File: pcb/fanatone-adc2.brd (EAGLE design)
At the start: 49 x 32 mm, 71 parts, among them IC1 OPA2134U, IC2 DIT4192-H, IC3 PCM4201-TSSOP-16, IC4 OPA2134U, Q1 SST5484, U1 OPA1612AID, U2 TPS62240DRVTG4

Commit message: Dickson charge pump layout, PCB wip, tidy up
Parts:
- removed C31: 0.1uF, SparkFun-Capacitors:0402-CAP
- added C33: 1uF, SparkFun-Passives:0805
- added D17: PMEG4005EJ, SparkFun-DiscreteSemi:SOD523
- added R10: 24k9, SparkFun-Passives:0603-RES
- added R9: 1M, SparkFun-Passives:0603-RES
- C22: value 1uF -> 1uF 16V
- C23: value 4.7uF 63V -> 4.7uF 16V
- D10, D11, D12, D13, D14, D15, D4, D5, D6, D7, D8, D9: device SparkFun-DiscreteSemi:SOD-323 -> SparkFun-DiscreteSemi:SOD523
- L1: value 4.7uH -> 1uH
- moved C32 134.6 mm to (74.7, 19.3), turned to 90 degrees
- moved C30 130.8 mm to (74.7, 22.9), turned to 270 degrees
- moved C25 124.1 mm to (85.1, 16.0), turned to 90 degrees
- moved U$5 123.7 mm to (71.9, 21.1), turned to 180 degrees
- moved C26 120.0 mm to (82.5, 16.0), turned to 90 degrees
- moved C29 119.5 mm to (74.9, 16.0), turned to 90 degrees
- moved D10 118.1 mm to (88.4, 14.2)
- moved C24 116.6 mm to (87.6, 16.0), turned to 90 degrees
- moved D12 116.4 mm to (83.3, 14.2)
- moved C27 116.0 mm to (80.0, 16.0), turned to 90 degrees
- moved C21 115.1 mm to (89.7, 10.9), turned to 270 degrees
- moved D14 115.1 mm to (78.2, 14.2)
- moved D9 112.9 mm to (88.4, 12.7), turned to 180 degrees
- moved C28 112.1 mm to (77.5, 16.0), turned to 90 degrees
- moved D11 112.0 mm to (85.9, 14.2)
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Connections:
- removed net N$35: C30.1, U$5.1
- new net N$32: C29.1, D15.C, D17.A
- net GND: now also C32.2, C33.2, R10.1
- net N$34: now also R10.2, R9.1, U$5.2; no longer U$5.8
- net N$38: now also D16.C
- net N$49: now also C33.1, D17.C, U$5.8; no longer C29.1, D15.C
- net VCAPSULE-RAW: now also C30.1, R9.2, U$5.1
- net VDPP: now also D16.A
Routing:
- net GND: track 57.0 -> 74.4 mm
- net N$34: track 0.00 -> 4.73 mm
- net N$38: track 0.00 -> 4.46 mm
- net N$48: track 0.00 -> 2.51 mm
- net N$46: track 0.00 -> 2.51 mm
- net N$41: track 0.00 -> 2.51 mm
- net N$47: track 0.00 -> 2.51 mm
- net N$43: track 0.00 -> 2.51 mm
- net N$32: track 0.00 -> 2.51 mm
- net N$29: track 0.00 -> 2.46 mm
- net N$36: track 0.00 -> 2.46 mm
- net N$33: track 0.00 -> 2.46 mm
- net N$27: track 0.00 -> 2.46 mm
- net N$13: track 0.00 -> 2.46 mm
- net VCAPSULE-RAW: track 8.09 -> 10.5 mm
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
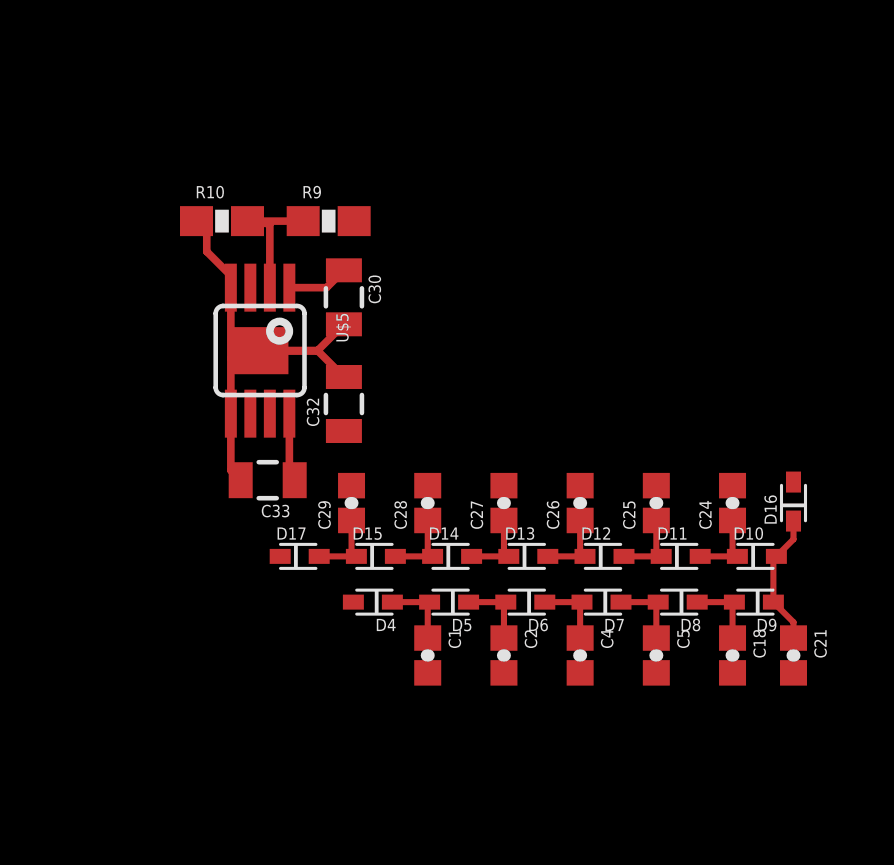
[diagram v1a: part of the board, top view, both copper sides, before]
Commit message: add concept for a MEMS Microphone array + step file sync + animation
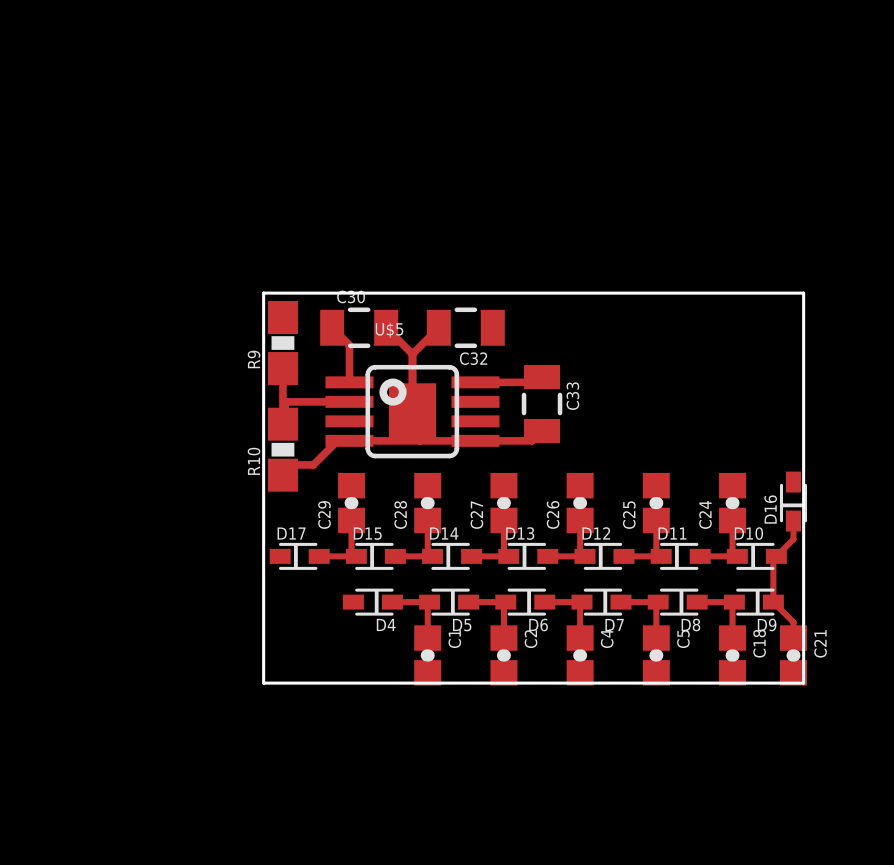
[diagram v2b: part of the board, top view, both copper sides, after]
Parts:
- moved C33 9.49 mm to (81.3, 19.3), turned to 270 degrees
- moved R10 7.89 mm to (72.6, 17.8), turned to 90 degrees
- moved U$5 5.47 mm to (77.0, 19.1), turned to 270 degrees
- moved C32 4.79 mm to (78.7, 21.8), turned to 180 degrees
- moved R9 4.34 mm to (72.6, 21.3), turned to 90 degrees
- moved C30 1.14 mm to (75.2, 21.8), turned to 0 degrees
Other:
- board size 49 x 32 mm -> 90 x 32 mm
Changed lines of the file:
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@@
 <setting verticaltext="up"/>
 </settings>
-<grid distance="0.125" unitdist="inch" unit="inch" style="lines" multiple="1" display="yes" altdistance="0.01" altunitdist="inch" altunit="inch"/>
+<grid distance="0.02" unitdist="inch" unit="inch" style="lines" multiple="1" display="yes" altdistance="0.01" altunitdist="inch" altunit="inch"/>
 <layers>
 <layer number="1" name="Top" color="39" fill="1" visible="yes" active="yes"/>
@@
 <wire x1="3.1" y1="32" x2="0" y2="28.9" width="0.1778" layer="20" curve="90"/>
 <wire x1="0" y1="3.1" x2="3.1" y2="0" width="0.1778" layer="20" curve="90"/>
+<wire x1="72" y1="23" x2="72" y2="10" width="0.1016" layer="20"/>
+<wire x1="72" y1="10" x2="90" y2="10" width="0.1016" layer="20"/>
+<wire x1="90" y1="10" x2="90" y2="23" width="0.1016" layer="20"/>
+<wire x1="90" y1="23" x2="72" y2="23" width="0.1016" layer="20"/>
+<dimension x1="90" y1="23" x2="72" y2="23" x3="81" y3="25" textsize="1.016" layer="20" precision="3" visible="yes"/>
+<dimension x1="90" y1="10" x2="90" y2="23" x3="93" y3="16.5" textsize="1.016" layer="20" precision="3" visible="yes"/>
 </plain>
 <attributes>
@@
 </element>
 <element name="D15" library="SparkFun-DiscreteSemi" package="SOD523" value="PMEG4005EJ" x="75.692" y="14.224"/>
-<element name="U$5" library="SparkFun-AnalogIC" package="POWER-SOP8" value="TPS7A4001" x="71.882" y="21.082" rot="R180"/>
-<element name="C30" library="SparkFun-Passives" package="0805" value="1uF" x="74.676" y="22.86" rot="R270"/>
+<element name="U$5" library="SparkFun-AnalogIC" package="POWER-SOP8" value="TPS7A4001" x="76.962" y="19.05" rot="R270"/>
+<element name="C30" library="SparkFun-Passives" package="0805" value="1uF" x="75.184" y="21.844"/>
 <element name="D16" library="SparkFun-DiscreteSemi" package="SOD523" value="" x="89.662" y="16.002" rot="R90"/>
-<element name="C32" library="SparkFun-Passives" package="0805" value="1uF 63V" x="74.676" y="19.304" rot="R90"/>
+<element name="C32" library="SparkFun-Passives" package="0805" value="1uF 63V" x="78.74" y="21.844" rot="R180"/>
 <element name="R8" library="SparkFun-Passives" package="0603-RES" value="100k" x="1.016" y="8.89" rot="R90"/>
-<element name="C33" library="SparkFun-Passives" package="0805" value="1uF" x="72.136" y="16.764" rot="R180"/>
+<element name="C33" library="SparkFun-Passives" package="0805" value="1uF" x="81.28" y="19.304" rot="R270"/>
 <element name="D17" library="SparkFun-DiscreteSemi" package="SOD523" value="PMEG4005EJ" x="73.152" y="14.224"/>
-<element name="R9" library="SparkFun-Passives" package="0603-RES" value="1M" x="74.168" y="25.4"/>
-<element name="R10" library="SparkFun-Passives" package="0603-RES" value="24k9" x="70.612" y="25.4"/>
+<element name="R9" library="SparkFun-Passives" package="0603-RES" value="1M" x="72.644" y="21.336" rot="R90"/>
+<element name="R10" library="SparkFun-Passives" package="0603-RES" value="24k9" x="72.644" y="17.78" rot="R90"/>
 </elements>
 <signals>
@@
 <contactref element="U$5" pad="4"/>
 <contactref element="R10" pad="1"/>
-<wire x1="71.236" y1="16.764" x2="70.907" y2="17.093" width="0.254" layer="1"/>
-<wire x1="70.907" y1="17.093" x2="70.907" y2="18.982" width="0.254" layer="1"/>
-<wire x1="70.907" y1="18.982" x2="70.907" y2="20.828" width="0.254" layer="1"/>
-<wire x1="70.907" y1="20.828" x2="70.907" y2="23.182" width="0.254" layer="1"/>
-<wire x1="71.882" y1="21.082" x2="71.161" y2="21.082" width="0.254" layer="1"/>
-<wire x1="71.161" y1="21.082" x2="70.907" y2="20.828" width="0.254" layer="1"/>
-<wire x1="74.676" y1="21.96" x2="73.798" y2="21.082" width="0.254" layer="1"/>
-<wire x1="73.798" y1="21.082" x2="71.882" y2="21.082" width="0.254" layer="1"/>
-<wire x1="74.676" y1="20.204" x2="73.798" y2="21.082" width="0.254" layer="1"/>
-<wire x1="73.798" y1="21.082" x2="71.882" y2="21.082" width="0.254" layer="1"/>
-<wire x1="70.907" y1="23.182" x2="70.907" y2="23.581" width="0.254" layer="1"/>
-<wire x1="70.907" y1="23.581" x2="70.104" y2="24.384" width="0.254" layer="1"/>
-<wire x1="70.104" y1="24.384" x2="70.104" y2="25.058" width="0.254" layer="1"/>
-<wire x1="70.104" y1="25.058" x2="69.762" y2="25.4" width="0.254" layer="1"/>
-<wire x1="47.128" y1="6.096" x2="70.907" y2="17.093" width="0" layer="19" extent="1-1"/>
+<wire x1="81.28" y1="18.404" x2="80.951" y2="18.075" width="0.254" layer="1"/>
+<wire x1="80.951" y1="18.075" x2="79.062" y2="18.075" width="0.254" layer="1"/>
+<wire x1="79.062" y1="18.075" x2="77.216" y2="18.075" width="0.254" layer="1"/>
+<wire x1="77.216" y1="18.075" x2="74.862" y2="18.075" width="0.254" layer="1"/>
+<wire x1="76.962" y1="19.05" x2="76.962" y2="18.329" width="0.254" layer="1"/>
+<wire x1="76.962" y1="18.329" x2="77.216" y2="18.075" width="0.254" layer="1"/>
+<wire x1="76.084" y1="21.844" x2="76.962" y2="20.966" width="0.254" layer="1"/>
+<wire x1="76.962" y1="20.966" x2="76.962" y2="19.05" width="0.254" layer="1"/>
+<wire x1="77.84" y1="21.844" x2="76.962" y2="20.966" width="0.254" layer="1"/>
+<wire x1="76.962" y1="20.966" x2="76.962" y2="19.05" width="0.254" layer="1"/>
+<wire x1="74.862" y1="18.075" x2="74.463" y2="18.075" width="0.254" layer="1"/>
+<wire x1="74.463" y1="18.075" x2="73.66" y2="17.272" width="0.254" layer="1"/>
+<wire x1="73.66" y1="17.272" x2="72.986" y2="17.272" width="0.254" layer="1"/>
+<wire x1="72.986" y1="17.272" x2="72.644" y2="16.93" width="0.254" layer="1"/>
+<wire x1="47.128" y1="6.096" x2="72.644" y2="16.93" width="0" layer="19" extent="1-1"/>
 <wire x1="3.048" y1="11.6475" x2="24.892" y2="16.256" width="0" layer="19" extent="1-1"/>
 </signal>
@@
 <contactref element="R8" pad="2"/>
 <contactref element="C32" pad="1"/>
-<wire x1="1.016" y1="11.6475" x2="74.676" y2="18.404" width="0" layer="19" extent="1-1"/>
+<wire x1="1.016" y1="11.6475" x2="79.64" y2="21.844" width="0" layer="19" extent="1-1"/>
 <wire x1="1.016" y1="9.74" x2="1.016" y2="11.6475" width="0" layer="19" extent="1-1"/>
 </signal>
@@
 <contactref element="D17" pad="C"/>
 <contactref element="C33" pad="1"/>
-<wire x1="73.036" y1="16.764" x2="72.857" y2="16.943" width="0.254" layer="1"/>
-<wire x1="72.857" y1="16.943" x2="72.857" y2="18.982" width="0.254" layer="1"/>
-<wire x1="72.552" y1="14.224" x2="73.036" y2="16.764" width="0" layer="19" extent="1-1"/>
+<wire x1="81.28" y1="20.204" x2="81.101" y2="20.025" width="0.254" layer="1"/>
+<wire x1="81.101" y1="20.025" x2="79.062" y2="20.025" width="0.254" layer="1"/>
+<wire x1="72.552" y1="14.224" x2="79.062" y2="20.025" width="0" layer="19" extent="1-1"/>
 </signal>
 <signal name="VCAPSULE-RAW">
@@
 <contactref element="R9" pad="2"/>
 <contactref element="U$5" pad="1"/>
-<wire x1="74.676" y1="23.76" x2="74.098" y2="23.182" width="0.254" layer="1"/>
-<wire x1="74.098" y1="23.182" x2="72.857" y2="23.182" width="0.254" layer="1"/>
-<wire x1="74.676" y1="23.76" x2="75.018" y2="25.4" width="0" layer="19" extent="1-1"/>
-<wire x1="41.402" y1="5.722" x2="72.857" y2="23.182" width="0" layer="19" extent="1-1"/>
+<wire x1="74.284" y1="21.844" x2="74.862" y2="21.266" width="0.254" layer="1"/>
+<wire x1="74.862" y1="21.266" x2="74.862" y2="20.025" width="0.254" layer="1"/>
+<wire x1="74.284" y1="21.844" x2="72.644" y2="22.186" width="0" layer="19" extent="1-1"/>
+<wire x1="41.402" y1="5.722" x2="72.644" y2="22.186" width="0" layer="19" extent="1-1"/>
 <wire x1="38.1" y1="5.334" x2="38.1" y2="5.588" width="0" layer="19" extent="1-1"/>
 <wire x1="1.016" y1="8.04" x2="38.1" y2="5.588" width="0" layer="19" extent="1-1"/>
@@
 <contactref element="R9" pad="1"/>
 <contactref element="R10" pad="2"/>
-<wire x1="73.318" y1="25.4" x2="71.462" y2="25.4" width="0.254" layer="1"/>
-<wire x1="72.207" y1="23.182" x2="72.207" y2="25.305" width="0.254" layer="1"/>
-<wire x1="72.207" y1="25.305" x2="71.462" y2="25.4" width="0.254" layer="1"/>
+<wire x1="72.644" y1="20.486" x2="72.644" y2="18.63" width="0.254" layer="1"/>
+<wire x1="74.862" y1="19.375" x2="72.739" y2="19.375" width="0.254" layer="1"/>
+<wire x1="72.739" y1="19.375" x2="72.644" y2="18.63" width="0.254" layer="1"/>
 </signal>
 </signals>
